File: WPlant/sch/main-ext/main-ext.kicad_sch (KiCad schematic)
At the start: 70 parts, among them J1 PROG/JTAG, J10 Ext, J8 eInk-Buttons, J9 Leak, M1 Motor_DC, Q6 Si2301, Q7 BC817, SW1 SW_Push, SW2 SW_Push, SW3 SW_Push, U1 SIWG917Y121MGABAR, U10 SP485EEN-L/TR, U11 TXU0102QDCURQ1, U5 TC4427AEOA713, U8 NC7S02P5, U9 INA180A2, X1 SIT1552AI-JE-DCC-32.768D

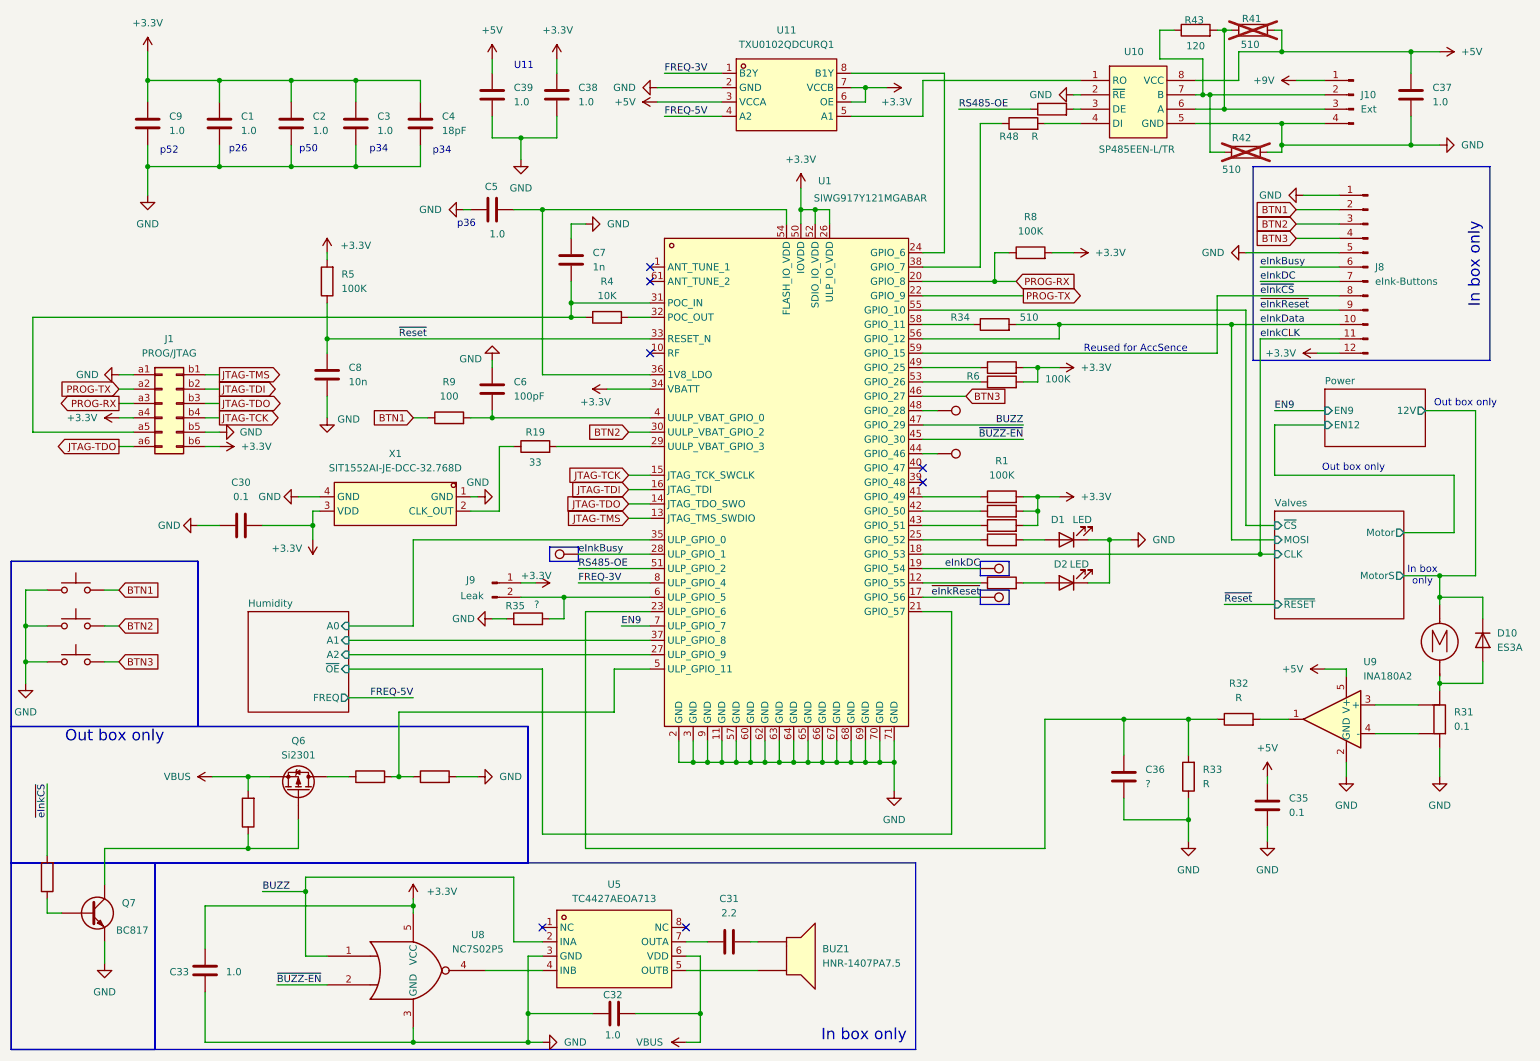
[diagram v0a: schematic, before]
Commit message: Generic design was splited to Main-Int and Main-Ext
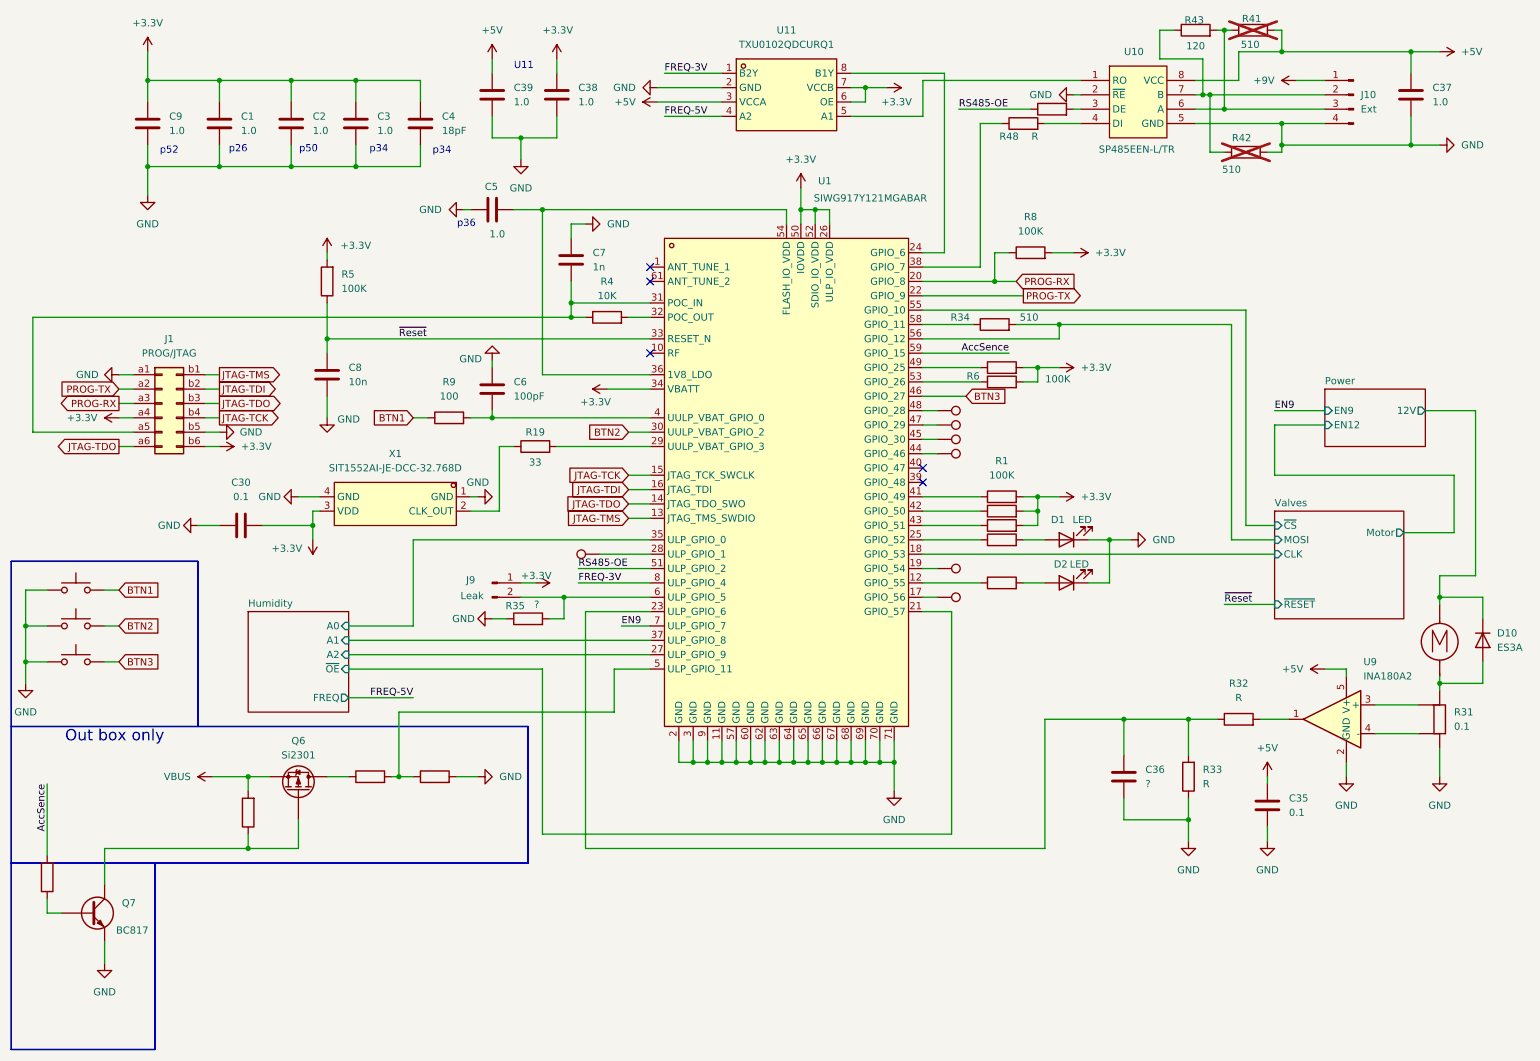
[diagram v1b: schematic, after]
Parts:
- removed BUZ1: HNR-1407PA7.5, easyeda2kicad:BUZ-TH_BD14.0-P7.60-D0.8-L, symbol easyeda2kicad:HNR-1407PA7.5
- removed C31: 2.2, Capacitor_SMD:C_0603_1608Metric_Pad1.08x0.95mm_HandSolder, symbol Device:C
- removed C32, C33: 1.0, Capacitor_SMD:C_0603_1608Metric_Pad1.08x0.95mm_HandSolder, symbol Device:C
- removed J8: eInk-Buttons, easyeda2kicad:CONN-TH_XAD-12A, symbol Connector:Conn_01x12_Pin
- removed U5: TC4427AEOA713, easyeda2kicad:SOIC-8_L4.9-W3.9-P1.27-LS6.0-BL, symbol easyeda2kicad:TC4427AEOA713
- removed U8: NC7S02P5, Package_TO_SOT_SMD:SOT-23-5_HandSoldering, symbol 74xGxx:74LVC1G02
- added TP6, TP7: TestPoint, TestPoint:TestPoint_Pad_1.0x1.0mm, symbol Connector:TestPoint
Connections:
- net BUZZ: no longer names the net of U1.47 (GPIO_29)
- net BUZZ: now also TP6.1
- net eInkBusy: no longer names the net of TP5.1, U1.28 (ULP_GPIO_1)
- net eInkCLK renamed Valves/CLK
- net eInkDC: no longer names the net of TP3.1, U1.19 (GPIO_54)
- net eInkData renamed Valves/MOSI
- net ~{BUZZ-EN}: no longer names the net of U1.45 (GPIO_30)
- net ~{BUZZ-EN}: now also TP7.1
- net ~{eInkCS} renamed AccSence
- net ~{eInkReset}: no longer names the net of TP4.1, U1.17 (GPIO_56)
- no-connect marks 7 -> 5
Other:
- sheet Valves ports: added none; removed MotorS
- note removed: "In box only"
- note removed: "Reused for AccSence"

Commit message: Update SWIG917 footprint. Change footprint of LeakDetector
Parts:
- J9: footprint Connector_PinHeader_2.54mm:PinHeader_1x02_P2.54mm_Vertical -> Connector_JST:JST_XH_B2B-XH-A_1x02_P2.50mm_Vertical
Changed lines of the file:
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@@
 			)
 		)
-		(property "Footprint" "Connector_PinHeader_2.54mm:PinHeader_1x02_P2.54mm_Vertical"
+		(property "Footprint" "Connector_JST:JST_XH_B2B-XH-A_1x02_P2.50mm_Vertical"
 			(at 100.33 113.03 0)
 			(effects

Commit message: Route of MainInt PCB done
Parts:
- J1: footprint locals:PinHeader_2x06_P2.54mm_HorizontalAB -> locals:PinHeader_2x06_P2.54mm_VerticalAB
- U1: footprint easyeda2kicad:COMM-SMD_SIWG917Y110LGNBA -> locals:COMM-SMD_SIWG917Y110LGNBA
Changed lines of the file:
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@@
 			)
 		)
-		(property "Footprint" "easyeda2kicad:COMM-SMD_SIWG917Y110LGNBA"
+		(property "Footprint" "locals:COMM-SMD_SIWG917Y110LGNBA"
 			(at 152.4 148.59 0)
 			(effects
@@
 			)
 		)
-		(property "Footprint" "locals:PinHeader_2x06_P2.54mm_HorizontalAB"
+		(property "Footprint" "locals:PinHeader_2x06_P2.54mm_VerticalAB"
 			(at 41.91 81.28 0)
 			(effects

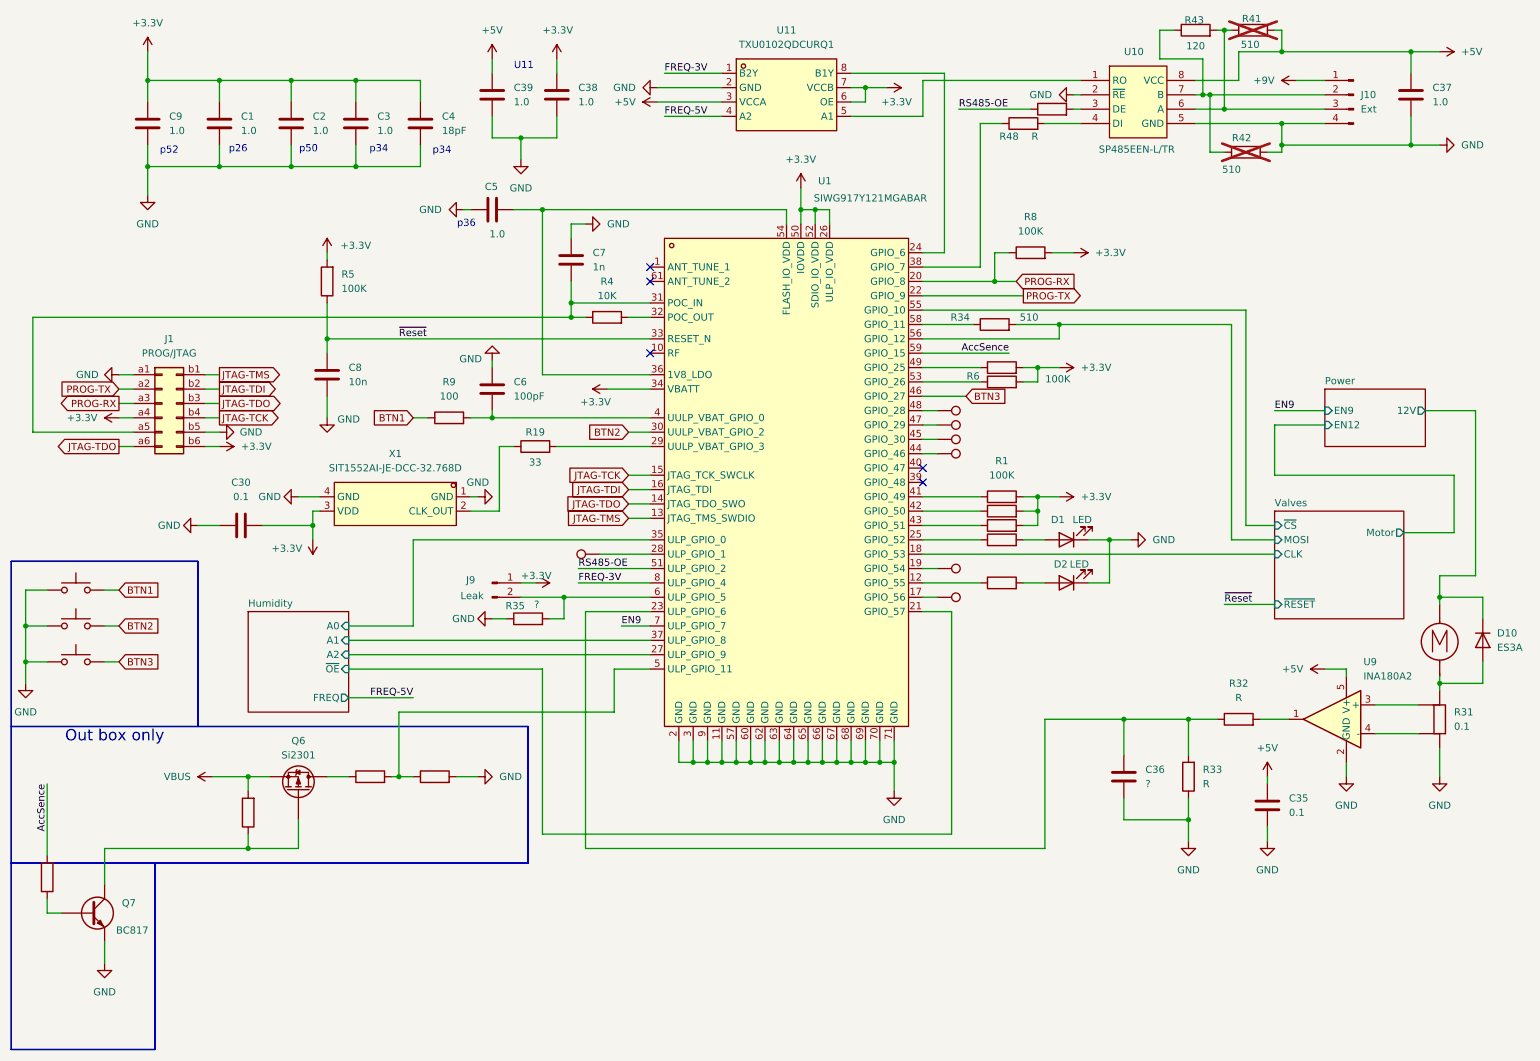
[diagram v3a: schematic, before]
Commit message: Route of MainExt PCB done
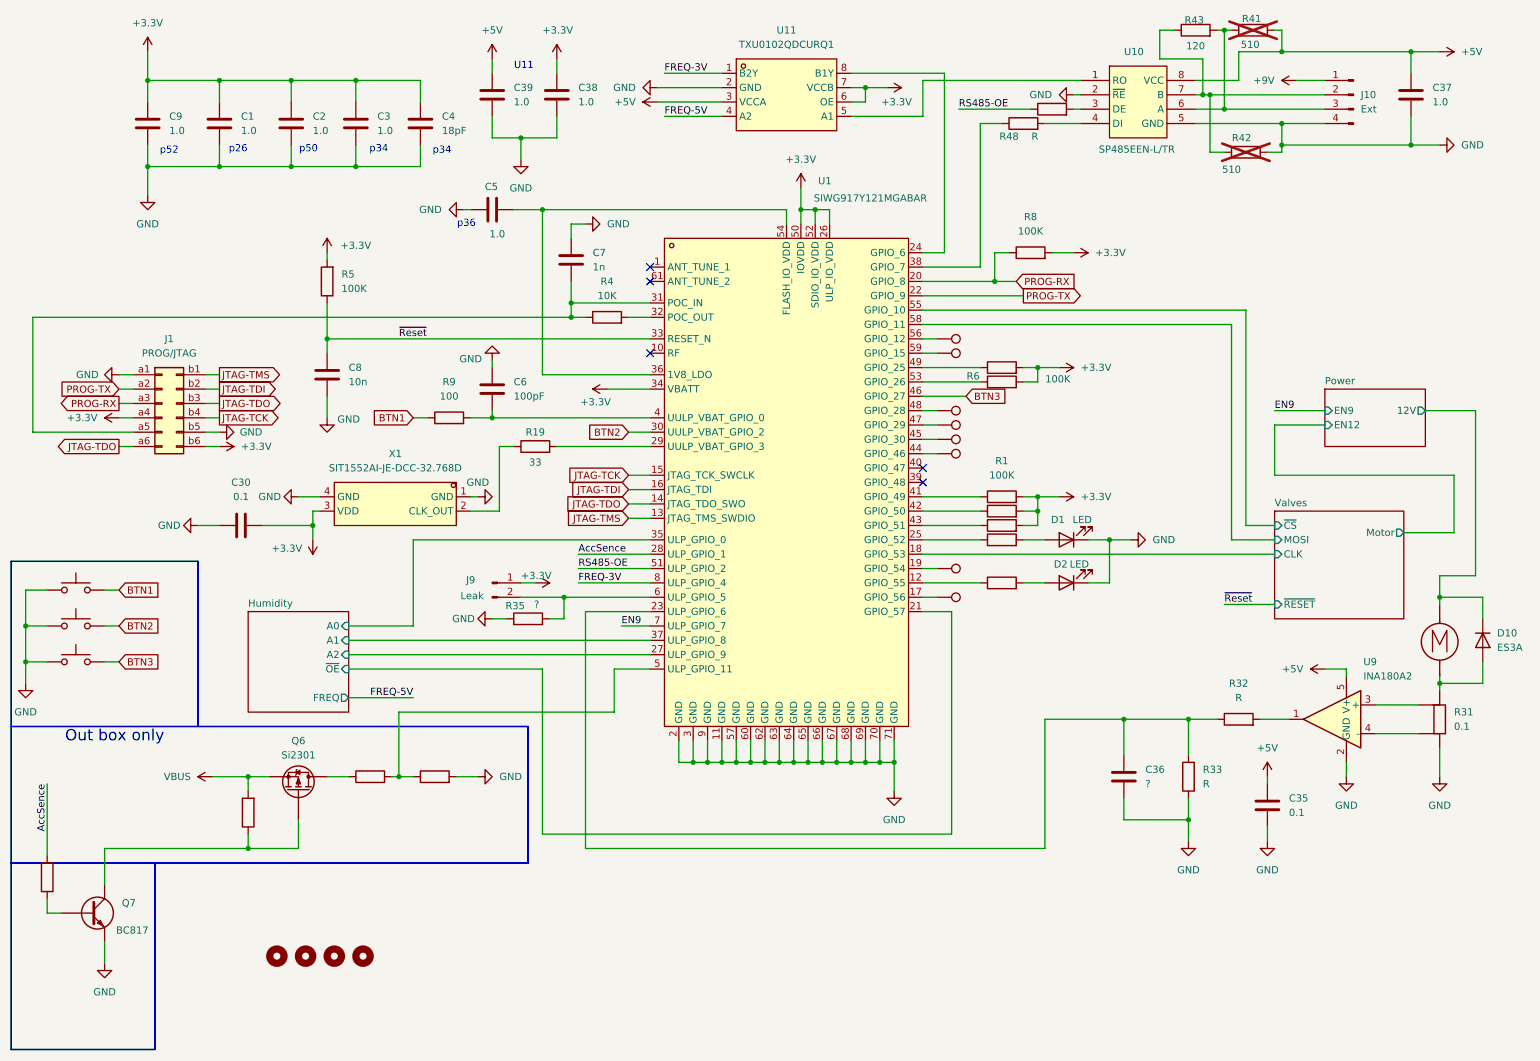
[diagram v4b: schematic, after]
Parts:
- removed R34: 510, Resistor_SMD:R_0603_1608Metric_Pad0.98x0.95mm_HandSolder, symbol Device:R
- added H1, H2, H3, H4: MountingHole, MountingHole:MountingHole_3.2mm_M3, symbol Mechanical:MountingHole
- added TP9: TestPoint, TestPoint:TestPoint_Pad_1.0x1.0mm, symbol Connector:TestPoint
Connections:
- net AccSence: now also U1.28 (ULP_GPIO_1); no longer U1.59 (GPIO_15)
- net Valves/MOSI: now also U1.58 (GPIO_11); no longer U1.56 (GPIO_12)
- net at TP5.1: now also U1.59 (GPIO_15); no longer U1.28 (ULP_GPIO_1)
- new net: TP9.1, U1.56 (GPIO_12)
